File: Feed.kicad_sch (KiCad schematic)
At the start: 35 parts

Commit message: feed update
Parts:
- removed CV26, CV27: ~, symbol PID_symbols:Check_Valve
- removed PT1 (x3): ~, symbol PID_symbols:Pressure_Transducer
- added HighFreq_PT, OX_Inj: ~, symbol PID_symbols:Pressure_Transducer
- added U72, U73: ~, symbol PID_symbols:stop
- gave numbers to parts that had none: 6
- renumbered Burst_Disc6 to Burst_Disc, CV28 to CV, PT1 to Chamber, Servo_Reg1 to EREG_Fuel, Engine4 to Engine, PT1 to FUELPT, T2 to Fuel, Needle_Valve1 to FuelFill_Needle_Valve, BV1 to FuelMain_BV, PT1 to Fuel_Inj, nO_Sol1 to Fuel_Vent_Sol, T1 to OX, PT1 to OXEREGPT, QD1 to OXFill_QD, BV1 to OXMain_BV, BV1 to OX_DipTube_BV, Servo_Reg1 to OX_EREG, nO_Sol1 to OX_Vent_Sol, SPRV12 to SPRV, SPRV11 to SPRV
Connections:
- net 1-2: now also FuelFill_Needle_Valve.
- net 1-4: now also n2_sol_vent., HighFreq_PT.; no longer Burst_Disc., CV., CV., Chamber., Engine., Fuel., FuelFill_Needle_Valve., Fuel_Inj., Fuel_Vent_Sol., OX., OXFill_QD., OX_Vent_Sol., SPRV., SPRV.
- net 3-4: now also U72., U73.
- net 3-8: now also CV., CV., EREG_Fuel., FUELPT., Fuel., Fuel_Vent_Sol., OX., OXEREGPT., OXFill_QD., OX_EREG., OX_Vent_Sol., SPRV., SPRV., U72.
- net D: now also Burst_Disc.; no longer FUELPT., OXEREGPT.
- net 1-8: now reaches Fuel_Inj.
- net 1-8: now also Chamber., Engine., OX_Inj., U73.
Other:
- note added: "3-4 INCH"
- moved on the sheet: Burst_Disc, Burst_Disc5, CV, Chamber, EREG_FuelA, Engine, FUELPT, FuelA, FuelFill_Needle_Valve, FuelMain_BV, Fuel_Inj, Fuel_Vent_Sol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

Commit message: more feed
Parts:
- added TC (x4): ~, symbol PID_symbols:Thermocouple
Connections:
- net D: now also FUELPT., HighFreq_PT., N2FILLPT., OXEREGPT., TC., TC., TC., TC.

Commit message: PT Removal
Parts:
- removed HighFreq_PT: ~, symbol PID_symbols:Pressure_Transducer
- removed TC: ~, symbol PID_symbols:Thermocouple
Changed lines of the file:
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@@
-	)
-	(junction
-		(at 106.68 88.9)
-		(diameter 0)
-		(color 0 0 0 0)
 	)
 	(junction
@@
 	(wire
 		(pts
-			(xy 106.68 85.09) (xy 106.68 88.9)
+			(xy 106.68 85.09) (xy 106.68 92.71)
 		)
 		(stroke
@@
 	(wire
 		(pts
-			(xy 115.57 88.9) (xy 106.68 88.9)
-		)
-		(stroke
-			(width 0)
-			(type default)
-		)
-	)
-	(wire
-		(pts
 			(xy 106.68 105.41) (xy 106.68 107.95)
 		)
@@
 	(wire
 		(pts
-			(xy 115.57 95.25) (xy 115.57 88.9)
-		)
-		(stroke
-			(width 0)
-			(type default)
-		)
-	)
-	(wire
-		(pts
 			(xy 106.68 165.1) (xy 120.65 165.1)
 		)
@@
 	(wire
 		(pts
-			(xy 115.57 100.33) (xy 115.57 102.87)
-		)
-		(stroke
-			(width 0)
-			(type default)
-		)
-	)
-	(wire
-		(pts
 			(xy 170.18 171.45) (xy 170.18 119.38)
 		)
@@
 		(pts
 			(xy 17.78 29.21) (xy 26.67 29.21)
-		)
-		(stroke
-			(width 0)
-			(type default)
-		)
-	)
-	(wire
-		(pts
-			(xy 106.68 88.9) (xy 106.68 92.71)
 		)
 		(stroke
@@
 				)
 				(justify right)
-				(hide yes)
-			)
-		)
-	)
-	(global_label "D"
-		(shape input)
-		(at 115.57 101.6 90)
-		(fields_autoplaced yes)
-		(effects
-			(font
-				(size 0.254 0.254)
-			)
-			(justify left)
-		)
-		(property "Intersheetrefs" "${INTERSHEET_REFS}"
-			(at 115.57 100.8794 90)
-			(effects
-				(font
-					(size 1.27 1.27)
-				)
-				(justify left)
 				(hide yes)
 			)
@@
 					(unit 1)
 				)
-			)
-		)
-	)
-	(symbol
-		(lib_name "Pressure_Transducer_1")
-		(lib_id "PID_symbols:Pressure_Transducer")
-		(at 115.57 97.79 90)
-		(unit 1)
-		(exclude_from_sim no)
-		(in_bom yes)
-		(on_board yes)
-		(dnp no)
-		(property "Reference" "HighFreq_PT"
-			(at 120.396 97.79 0)
-			(effects
-				(font
-					(size 1.27 1.27)
-				)
-			)
-		)
-		(property "Value" "~"
-			(at 116.84 97.79 0)
-			(effects
-				(font
-					(size 1.27 1.27)
-				)
-				(hide yes)
-			)
-		)
-		(property "Footprint" ""
-			(at 115.57 97.79 0)
-			(effects
-				(font
-					(size 1.27 1.27)
-				)
-				(hide yes)
-			)
-		)
-		(property "Datasheet" ""
-			(at 115.57 97.79 0)
-			(effects
-				(font
-					(size 1.27 1.27)
-				)
-				(hide yes)
-			)
-		)
-		(property "Description" ""
-			(at 115.57 97.79 0)
-			(effects
-				(font
-					(size 1.27 1.27)
-				)
-			)
-		)
-		(pin ""
-		)
-		(pin ""
-		)
-		(pin ""
-		)
-		(instances
-			(project "P_IDs"
-				(path "/045f1f05-3134-4b6d-91b6-463031104f1e/a0b6300e-76e9-4a18-afd6-e2d656b0d8f9/ac6f9866-6d7d-491d-94a4-140f8922d2b9"
-					(reference "HighFreq_PT")
-					(unit 1)
-				)
-			)
-		)
-	)
-	(symbol
-		(lib_id "PID_symbols:Thermocouple")
-		(at 115.57 105.41 0)
-		(unit 1)
-		(exclude_from_sim no)
-		(in_bom yes)
-		(on_board yes)
-		(dnp no)
-		(fields_autoplaced yes)
-		(property "Reference" "TC"
-			(at 118.11 106.0449 0)
-			(effects
-				(font
-					(size 1.27 1.27)
-				)
-				(justify left)
-			)
-		)
-		(property "Value" "~"
-			(at 115.57 105.41 0)
-			(effects
-				(font
-					(size 1.27 1.27)
-				)
-				(hide yes)
-			)
-		)
-		(property "Footprint" ""
-			(at 115.57 105.41 0)
-			(effects
-				(font
-					(size 1.27 1.27)
-				)
-				(hide yes)
-			)
-		)
-		(property "Datasheet" ""
-			(at 115.57 105.41 0)
-			(effects
-				(font
-					(size 1.27 1.27)
-				)
-				(hide yes)
-			)
-		)
-		(property "Description" ""
-			(at 115.57 105.41 0)
-			(effects
-				(font
-					(size 1.27 1.27)
-				)
-			)
-		)
-		(pin ""
-		)
-		(instances
-			(project "P_IDs"
-				(path "/045f1f05-3134-4b6d-91b6-463031104f1e/a0b6300e-76e9-4a18-afd6-e2d656b0d8f9/ac6f9866-6d7d-491d-94a4-140f8922d2b9"
-					(reference "TC")
-					(unit 1)
-				)

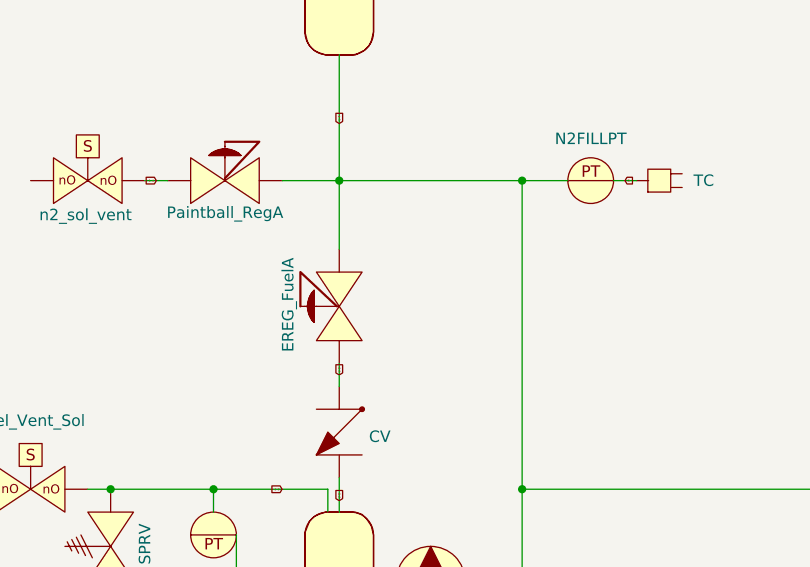
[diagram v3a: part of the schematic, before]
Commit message: Revert "PT Removal"
This reverts commit 88dc120e411422b574d6687b84eec723b5fabe79.
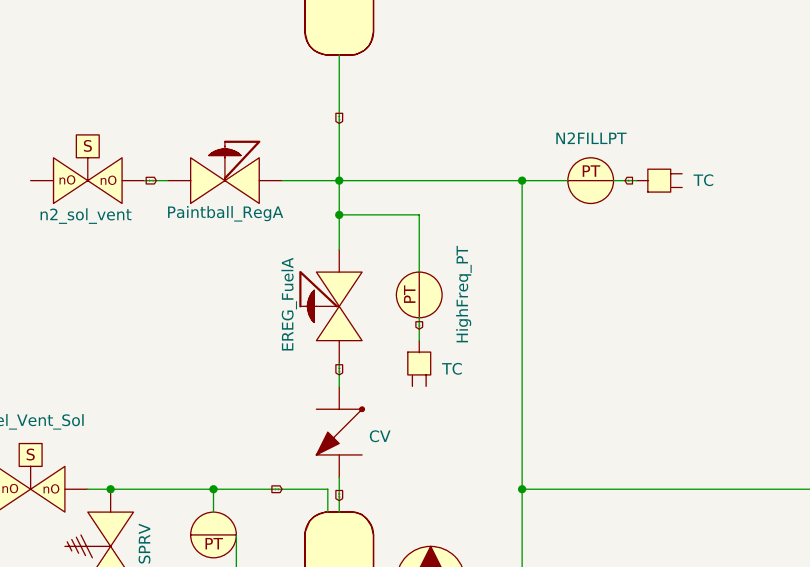
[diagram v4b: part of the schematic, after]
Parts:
- added HighFreq_PT: ~, symbol PID_symbols:Pressure_Transducer
- added TC: ~, symbol PID_symbols:Thermocouple
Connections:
- net 1-4: now also HighFreq_PT.
- net D: now also HighFreq_PT., TC.
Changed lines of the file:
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@@
+	)
+	(junction
+		(at 106.68 88.9)
+		(diameter 0)
+		(color 0 0 0 0)
 	)
 	(junction
@@
 	(wire
 		(pts
-			(xy 106.68 85.09) (xy 106.68 92.71)
+			(xy 106.68 85.09) (xy 106.68 88.9)
 		)
 		(stroke
@@
 	(wire
 		(pts
+			(xy 115.57 88.9) (xy 106.68 88.9)
+		)
+		(stroke
+			(width 0)
+			(type default)
+		)
+	)
+	(wire
+		(pts
 			(xy 106.68 105.41) (xy 106.68 107.95)
 		)
@@
 	(wire
 		(pts
+			(xy 115.57 95.25) (xy 115.57 88.9)
+		)
+		(stroke
+			(width 0)
+			(type default)
+		)
+	)
+	(wire
+		(pts
 			(xy 106.68 165.1) (xy 120.65 165.1)
 		)
@@
 	(wire
 		(pts
+			(xy 115.57 100.33) (xy 115.57 102.87)
+		)
+		(stroke
+			(width 0)
+			(type default)
+		)
+	)
+	(wire
+		(pts
 			(xy 170.18 171.45) (xy 170.18 119.38)
 		)
@@
 		(pts
 			(xy 17.78 29.21) (xy 26.67 29.21)
+		)
+		(stroke
+			(width 0)
+			(type default)
+		)
+	)
+	(wire
+		(pts
+			(xy 106.68 88.9) (xy 106.68 92.71)
 		)
 		(stroke
@@
 				)
 				(justify right)
+				(hide yes)
+			)
+		)
+	)
+	(global_label "D"
+		(shape input)
+		(at 115.57 101.6 90)
+		(fields_autoplaced yes)
+		(effects
+			(font
+				(size 0.254 0.254)
+			)
+			(justify left)
+		)
+		(property "Intersheetrefs" "${INTERSHEET_REFS}"
+			(at 115.57 100.8794 90)
+			(effects
+				(font
+					(size 1.27 1.27)
+				)
+				(justify left)
 				(hide yes)
 			)
@@
 					(unit 1)
 				)
+			)
+		)
+	)
+	(symbol
+		(lib_name "Pressure_Transducer_1")
+		(lib_id "PID_symbols:Pressure_Transducer")
+		(at 115.57 97.79 90)
+		(unit 1)
+		(exclude_from_sim no)
+		(in_bom yes)
+		(on_board yes)
+		(dnp no)
+		(property "Reference" "HighFreq_PT"
+			(at 120.396 97.79 0)
+			(effects
+				(font
+					(size 1.27 1.27)
+				)
+			)
+		)
+		(property "Value" "~"
+			(at 116.84 97.79 0)
+			(effects
+				(font
+					(size 1.27 1.27)
+				)
+				(hide yes)
+			)
+		)
+		(property "Footprint" ""
+			(at 115.57 97.79 0)
+			(effects
+				(font
+					(size 1.27 1.27)
+				)
+				(hide yes)
+			)
+		)
+		(property "Datasheet" ""
+			(at 115.57 97.79 0)
+			(effects
+				(font
+					(size 1.27 1.27)
+				)
+				(hide yes)
+			)
+		)
+		(property "Description" ""
+			(at 115.57 97.79 0)
+			(effects
+				(font
+					(size 1.27 1.27)
+				)
+			)
+		)
+		(pin ""
+		)
+		(pin ""
+		)
+		(pin ""
+		)
+		(instances
+			(project "P_IDs"
+				(path "/045f1f05-3134-4b6d-91b6-463031104f1e/a0b6300e-76e9-4a18-afd6-e2d656b0d8f9/ac6f9866-6d7d-491d-94a4-140f8922d2b9"
+					(reference "HighFreq_PT")
+					(unit 1)
+				)
+			)
+		)
+	)
+	(symbol
+		(lib_id "PID_symbols:Thermocouple")
+		(at 115.57 105.41 0)
+		(unit 1)
+		(exclude_from_sim no)
+		(in_bom yes)
+		(on_board yes)
+		(dnp no)
+		(fields_autoplaced yes)
+		(property "Reference" "TC"
+			(at 118.11 106.0449 0)
+			(effects
+				(font
+					(size 1.27 1.27)
+				)
+				(justify left)
+			)
+		)
+		(property "Value" "~"
+			(at 115.57 105.41 0)
+			(effects
+				(font
+					(size 1.27 1.27)
+				)
+				(hide yes)
+			)
+		)
+		(property "Footprint" ""
+			(at 115.57 105.41 0)
+			(effects
+				(font
+					(size 1.27 1.27)
+				)
+				(hide yes)
+			)
+		)
+		(property "Datasheet" ""
+			(at 115.57 105.41 0)
+			(effects
+				(font
+					(size 1.27 1.27)
+				)
+				(hide yes)
+			)
+		)
+		(property "Description" ""
+			(at 115.57 105.41 0)
+			(effects
+				(font
+					(size 1.27 1.27)
+				)
+			)
+		)
+		(pin ""
+		)
+		(instances
+			(project "P_IDs"
+				(path "/045f1f05-3134-4b6d-91b6-463031104f1e/a0b6300e-76e9-4a18-afd6-e2d656b0d8f9/ac6f9866-6d7d-491d-94a4-140f8922d2b9"
+					(reference "TC")
+					(unit 1)
+				)
